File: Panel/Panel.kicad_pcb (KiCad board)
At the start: 2 copper layers, 100 x 100 mm, 76 parts, among them J1 Conn_01x03, J10 Conn_01x02, J11 Conn_01x03, J12 Conn_01x03, J2 USB_C_Receptacle_USB2.0, J3 Conn_01x02, J4 Conn_02x06_Odd_Even, J5 Conn_01x07, J6 Conn_01x02, J7 Conn_01x02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

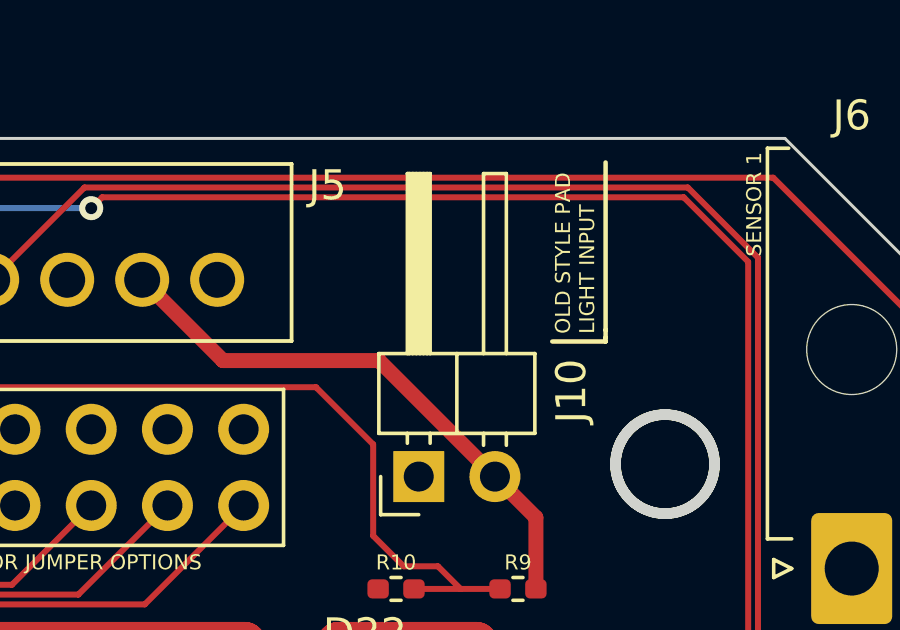
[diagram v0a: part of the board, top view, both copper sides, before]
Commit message: Add more labels to PCB silkscreen, update README
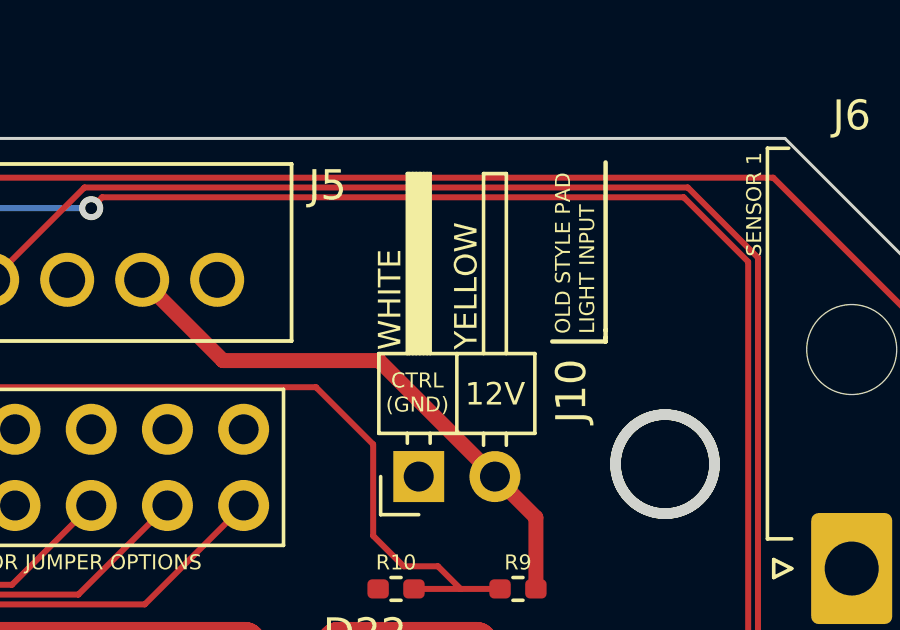
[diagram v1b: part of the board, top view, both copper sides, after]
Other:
- board text added: "12V"
- board text added: "CTRL (GND)"
- board text added: "WHITE"
- board text added: "YELLOW"
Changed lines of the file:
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@@
       (drillshape 0)
       (scaleselection 1)
-      (outputdirectory "Assembly")
+      (outputdirectory "Gerber/")
     )
   )
@@
     (effects (font (size 0.5 0.5) (thickness 0.125)))
   )
+  (gr_text "WHITE" (at 160.8328 55.372 90) (layer "F.SilkS")
+    (effects (font (size 0.75 0.75) (thickness 0.15)))
+  )
   (gr_text "RESET" (at 138.176 59.309 90) (layer "F.SilkS")
     (effects (font (size 0.75 0.75) (thickness 0.15)))
   )
+  (gr_text "CTRL\n(GND)" (at 161.7472 58.4708) (layer "F.SilkS")
+    (effects (font (size 0.5 0.5) (thickness 0.125)))
+  )
   (gr_text "SENSOR 4" (at 82.296 104.267) (layer "F.SilkS")
     (effects (font (size 0.5 0.5) (thickness 0.125)))
@@
     (effects (font (size 0.75 0.75) (thickness 0.15)))
   )
+  (gr_text "YELLOW" (at 163.3728 54.9148 90) (layer "F.SilkS")
+    (effects (font (size 0.75 0.75) (thickness 0.15)))
+  )
   (gr_text "OLD STYLE PAD\nLIGHT INPUT" (at 167.005 56.515 90) (layer "F.SilkS")
     (effects (font (size 0.5 0.5) (thickness 0.125)) (justify left))
@@
     (effects (font (size 0.5 0.5) (thickness 0.125)))
   )
+  (gr_text "12V" (at 164.338 58.5216) (layer "F.SilkS")
+    (effects (font (size 0.75 0.75) (thickness 0.15)))
+  )
   (gr_text "SENSOR 3" (at 86.995 147.701 270) (layer "F.SilkS")

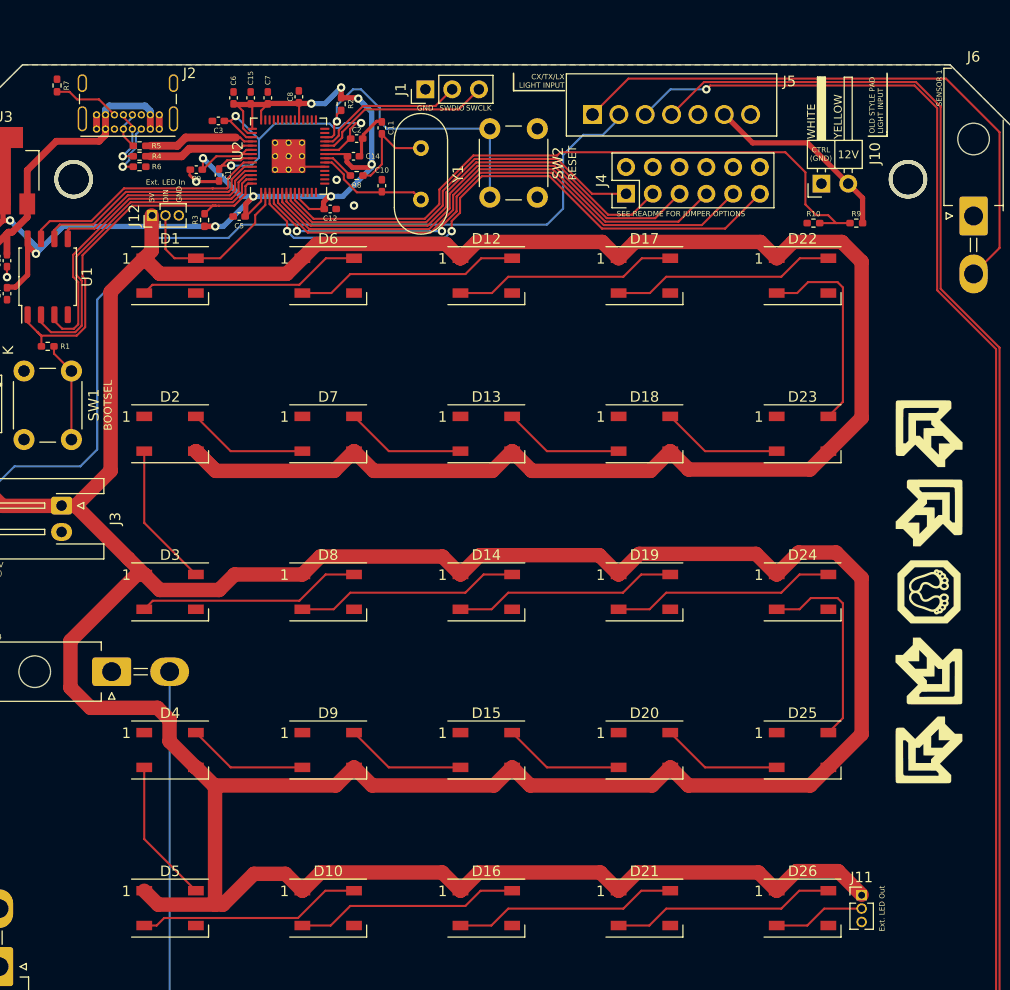
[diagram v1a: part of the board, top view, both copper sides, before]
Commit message: Fix critical issue - KiCad assigned LED pins wrong
This would result in any boards manufactured with this design being unusable without cutting traces and bodging connections.
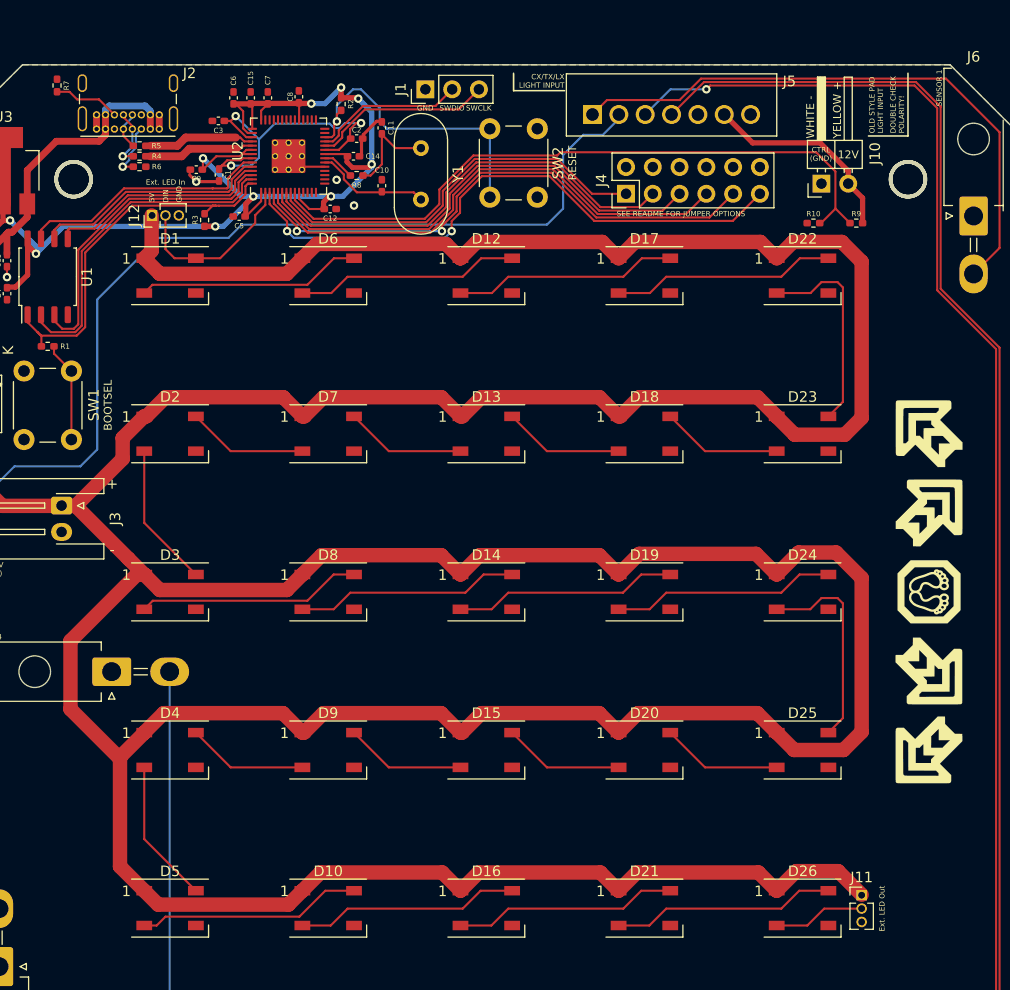
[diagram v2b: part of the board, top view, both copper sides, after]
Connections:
- D13 pad 1: GND -> Ext 5V
- D13 pad 3: Ext 5V -> GND
- D15 pad 1: GND -> Ext 5V
- D15 pad 3: Ext 5V -> GND
- D18 pad 1: GND -> Ext 5V
- D18 pad 3: Ext 5V -> GND
- D2 pad 1: GND -> Ext 5V
- D2 pad 3: Ext 5V -> GND
- D20 pad 1: GND -> Ext 5V
- D20 pad 3: Ext 5V -> GND
- D23 pad 1: GND -> Ext 5V
- D23 pad 3: Ext 5V -> GND
- D25 pad 1: GND -> Ext 5V
- D25 pad 3: Ext 5V -> GND
- D4 pad 1: GND -> Ext 5V
- D4 pad 3: Ext 5V -> GND
- D7 pad 1: GND -> Ext 5V
- D7 pad 3: Ext 5V -> GND
- D9 pad 1: GND -> Ext 5V
- D9 pad 3: Ext 5V -> GND
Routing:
- net Ext 5V: track 495.4 -> 482.3 mm
- net GPIO7: track 63.7 -> 64.5 mm
- net LIGHT EN: track 18.8 -> 19.5 mm
- net GPIO4: track 46.0 -> 45.4 mm
- net GPIO5: track 42.8 -> 42.2 mm
- net GPIO3: track 49.2 -> 48.6 mm
- net GPIO2: track 52.7 -> 52.1 mm
- net GPIO1: track 56.7 -> 56.1 mm
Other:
- board text added: "+"
- board text added: "-"
- board text added: "DOUBLE CHECK POLARITY!"
- board text added: "WHITE -"
- board text added: "YELLOW +"
- board text removed: "WHITE"
- board text removed: "YELLOW"

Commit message: Tidy up routing
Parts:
- moved J3 1.60 mm to (88.1, 91.8)
- moved J9 1.02 mm to (94.5, 106.6)
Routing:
- net SENSOR 4: track 240.7 -> 98.8 mm, vias 2 -> 0
- net Ext 5V: track 482.3 -> 459.6 mm
- net SENSOR 1: track 56.6 -> 49.7 mm
- net SENSOR 2: track 141.4 -> 138.1 mm

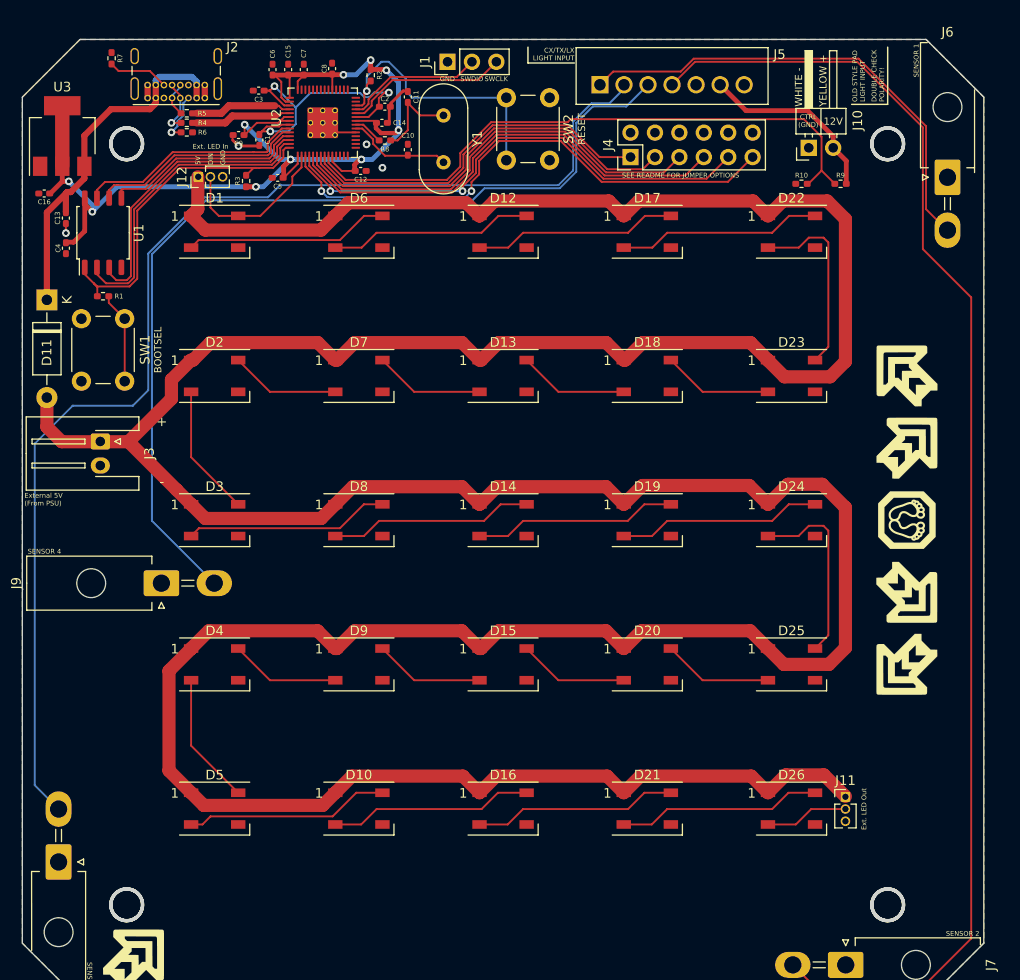
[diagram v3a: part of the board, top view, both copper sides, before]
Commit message: Fix hole alignment, tidy more routing
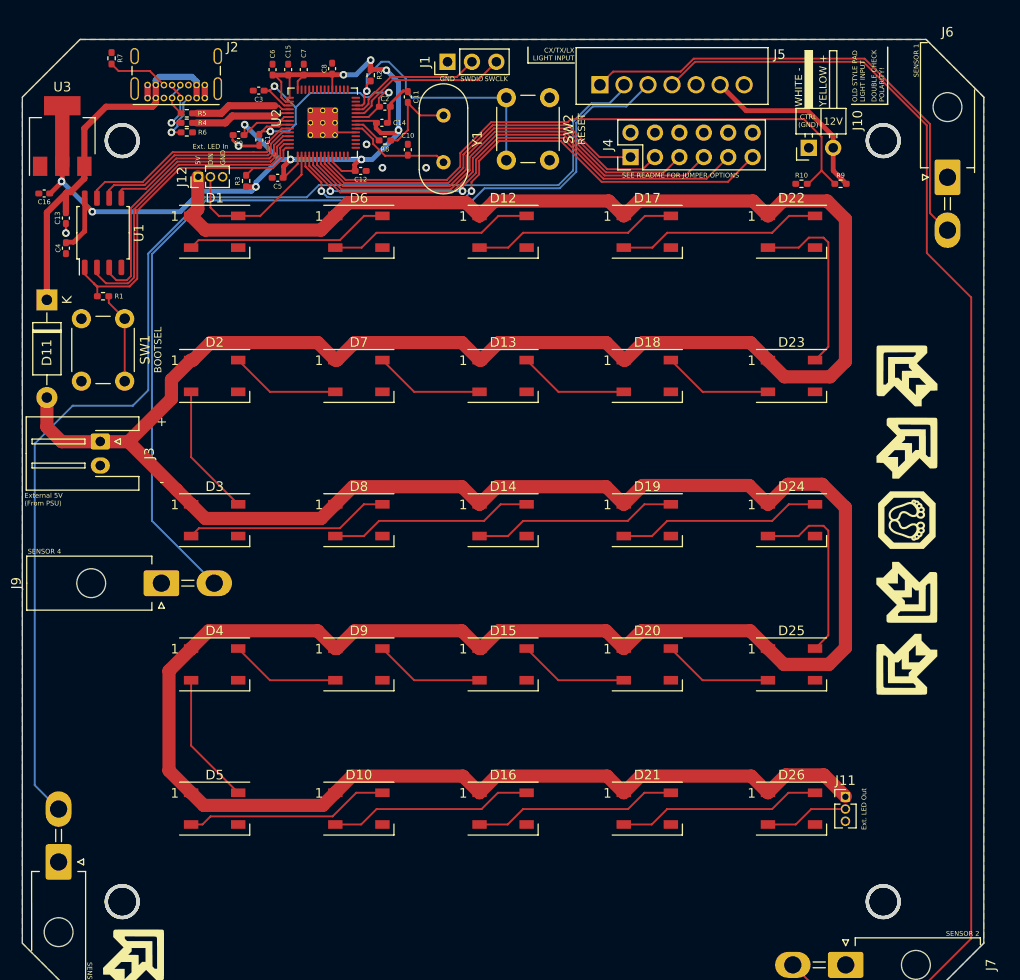
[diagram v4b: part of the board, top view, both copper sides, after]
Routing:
- net GND: vias 4 -> 5
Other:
- outline, holes or cut-outs redrawn
- board text added: "Overkill PIU Pad Lighting Kit Rev. 2"
- board text removed: "Overkill PIU Pad Lighting Kit"

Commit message: Minor changes
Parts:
- added G***: LOGO, LogoFootprints:Arrow_15mm, B.Cu at (113.0, 99.9)
- added G***: LOGO, LogoFootprints:Arrow_15mm, B.Cu at (147.0, 99.9)
- added G***: LOGO, LogoFootprints:Arrow_15mm, B.Cu at (164.0, 99.9)
- added G***: LOGO, LogoFootprints:CenterStep_15mm, B.Cu at (130.0, 99.9)
- added G***: LOGO, LogoFootprints:Arrow_15mm, B.Cu at (96.0, 99.9)

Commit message: Hopefully final nitpicks and adjustments
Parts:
- moved J1 2.55 mm to (121.7, 52.3)
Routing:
- net SWDIO: track 14.4 -> 11.9 mm
- net SWCLK: track 17.2 -> 14.7 mm
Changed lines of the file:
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@@
   )
   (footprint "Connector_PinHeader_2.54mm:PinHeader_1x03_P2.54mm_Vertical" (layer "F.Cu")
-    (at 124.221 52.324 90)
+    (at 121.673736 52.324 90)
     (descr "Through hole straight pin header, 1x03, 2.54mm pitch, single row")
     (tags "Through hole pin header THT 1x03 2.54mm single row")
@@
     (effects (font (size 0.5 0.5) (thickness 0.125)) (justify left))
   )
-  (gr_text "SWDIO" (at 126.746 54.102) (layer "F.SilkS")
+  (gr_text "SWDIO" (at 124.206 54.102) (layer "F.SilkS")
     (effects (font (size 0.5 0.5) (thickness 0.125)))
   )
-  (gr_text "SWCLK\n" (at 129.286 54.102) (layer "F.SilkS")
+  (gr_text "SWCLK\n" (at 126.746 54.102) (layer "F.SilkS")
     (effects (font (size 0.5 0.5) (thickness 0.125)))
   )
-  (gr_text "GND" (at 124.206 54.102) (layer "F.SilkS")
+  (gr_text "GND" (at 121.666 54.102) (layer "F.SilkS")
     (effects (font (size 0.5 0.5) (thickness 0.125)))
   )
@@
   (segment (start 84.526188 69.2075) (end 84.526188 70.135188) (width 0.2) (layer "F.Cu") (net 2))
   (segment (start 118.3311 56.9976) (end 118.1608 57.1679) (width 0.3) (layer "F.Cu") (net 2))
-  (segment (start 102.4815 61.0795) (end 101.8615 60.4595) (width 0.3) (layer "F.Cu") (net 2))
   (segment (start 98.975 56.095) (end 98.975 54.745) (width 0.65) (layer "F.Cu") (net 2))
-  (segment (start 101.8615 60.4595) (end 101.8615 59.944) (width 0.2) (layer "F.Cu") (net 2))
   (segment (start 118.1608 57.1679) (end 118.1608 58.5724) (width 0.3) (layer "F.Cu") (net 2))
   (segment (start 118.1608 58.5724) (end 118.0592 58.674) (width 0.3) (layer "F.Cu") (net 2))
-  (segment (start 114.677472 59.6655) (end 112.789972 59.6655) (width 0.2) (layer "F.Cu") (net 2))
+  (segment (start 102.266 61.0795) (end 101.9215 60.735) (width 0.3) (layer "F.Cu") (net 2))
   (segment (start 104.648 61.0795) (end 102.4815 61.0795) (width 0.3) (layer "F.Cu") (net 2))
+  (segment (start 114.677472 59.6655) (end 112.789972 59.6655) (width 0.2) (layer "F.Cu") (net 2))
+  (segment (start 101.9215 60.735) (end 101.9215 59.944) (width 0.3) (layer "F.Cu") (net 2))
   (segment (start 93.025 56.095) (end 93.025 54.745) (width 0.65) (layer "F.Cu") (net 2))
   (segment (start 118.3311 56.9976) (end 118.3311 56.6241) (width 0.3) (layer "F.Cu") (net 2))
@@
   (segment (start 84.526188 70.135188) (end 84.5312 70.1402) (width 0.2) (layer "F.Cu") (net 2))
   (segment (start 118.3311 56.6241) (end 119.6011 55.3541) (width 0.3) (layer "F.Cu") (net 2))
+  (segment (start 102.4815 61.0795) (end 102.266 61.0795) (width 0.3) (layer "F.Cu") (net 2))
   (via (at 121.9962 63.3476) (size 0.8) (drill 0.4) (layers "F.Cu" "B.Cu") (free) (net 2))
   (via (at 115.7986 60.9092) (size 0.8) (drill 0.4) (layers "F.Cu" "B.Cu") (free) (net 2))
@@
   (segment (start 164.333 60.066) (end 164.333 61.271) (width 0.5) (layer "F.Cu") (net 62))
   (segment (start 164.333 63.651126) (end 165.6975 65.015626) (width 0.5) (layer "F.Cu") (net 62))
-  (segment (start 116.003 56.717) (end 116.003 56.209) (width 0.2) (layer "F.Cu") (net 85))
-  (segment (start 115.4545 57.2655) (end 116.003 56.717) (width 0.2) (layer "F.Cu") (net 85))
-  (segment (start 118.31 53.902) (end 125.183 53.902) (width 0.2) (layer "F.Cu") (net 85))
   (segment (start 114.677472 57.2655) (end 115.4545 57.2655) (width 0.2) (layer "F.Cu") (net 85))
-  (segment (start 125.183 53.902) (end 126.761 52.324) (width 0.2) (layer "F.Cu") (net 85))
   (segment (start 116.003 56.209) (end 118.31 53.902) (width 0.2) (layer "F.Cu") (net 85))
-  (segment (start 127.396 54.229) (end 129.301 52.324) (width 0.2) (layer "F.Cu") (net 86))
-  (segment (start 116.33 56.898) (end 116.33 56.39) (width 0.2) (layer "F.Cu") (net 86))
-  (segment (start 114.5615 57.6655) (end 115.5625 57.6655) (width 0.2) (layer "F.Cu") (net 86))
+  (segment (start 122.635736 53.902) (end 124.213736 52.324) (width 0.2) (layer "F.Cu") (net 85))
+  (segment (start 118.31 53.902) (end 122.635736 53.902) (width 0.2) (layer "F.Cu") (net 85))
+  (segment (start 116.003 56.717) (end 116.003 56.209) (width 0.2) (layer "F.Cu") (net 85))
+  (segment (start 115.4545 57.2655) (end 116.003 56.717) (width 0.2) (layer "F.Cu") (net 85))
   (segment (start 115.5625 57.6655) (end 116.33 56.898) (width 0.2) (layer "F.Cu") (net 86))
-  (segment (start 118.491 54.229) (end 127.396 54.229) (width 0.2) (layer "F.Cu") (net 86))
+  (segment (start 124.848736 54.229) (end 126.753736 52.324) (width 0.2) (layer "F.Cu") (net 86))
+  (segment (start 114.5615 57.6655) (end 115.5625 57.6655) (width 0.2) (layer "F.Cu") (net 86))
+  (segment (start 116.33 56.898) (end 116.33 56.39) (width 0.2) (layer "F.Cu") (net 86))
   (segment (start 116.33 56.39) (end 118.491 54.229) (width 0.2) (layer "F.Cu") (net 86))
+  (segment (start 118.491 54.229) (end 124.848736 54.229) (width 0.2) (layer "F.Cu") (net 86))
   (zone (net 2) (net_name "GND") (layers F&B.Cu) (hatch edge 0.508)
     (connect_pads (clearance 0.508))
